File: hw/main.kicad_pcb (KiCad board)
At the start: 2 copper layers, 110 x 85 mm, 106 parts, among them J1 UART_01X03, J2 SWD_01X04, J3 SWD_01X04, J4 IDC_02X07, J5 IDC_02X07, J6 IDC_02X03, J7 IDC_02X13, J8 SMA, J9 IDC_02X05, SW1 LCD_BTN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

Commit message: updated pcb
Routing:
- net +5V: track 313.4 -> 312.7 mm

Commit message: updated pcb
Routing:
- net /Back/LED_PWM_R: track 239.6 -> 254.1 mm, vias 4 -> 8
- net /Back/LED_PWM_B: track 238.3 -> 246.7 mm, vias 7 -> 13
- net /Back/LED_PWM_G: track 225.5 -> 232.0 mm, vias 7 -> 13
- net +5V: track 312.7 -> 311.9 mm

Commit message: updated pcb
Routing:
- net +5V5: track 109.9 -> 107.6 mm

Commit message: updated pcb
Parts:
- added G***: LOGO, KLIB_Logo:wykys_skill, F.Cu at (147.0, 110.0)
- added REF**: Fiducial_Pad_1mm_Outer_2mm, KLIB_Mechanical:Fiducial_Pad_1mm_Outer_2mm, F.Cu at (190.0, 110.0)
- added REF**: Fiducial_Pad_1mm_Outer_2mm, KLIB_Mechanical:Fiducial_Pad_1mm_Outer_2mm, F.Cu at (190.0, 45.0)
- added REF**: Fiducial_Pad_1mm_Outer_2mm, KLIB_Mechanical:Fiducial_Pad_1mm_Outer_2mm, F.Cu at (90.0, 45.0)
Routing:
- net GND: vias 74 -> 78
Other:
- board text added: "LASER GAME MAIN BOARD V2"

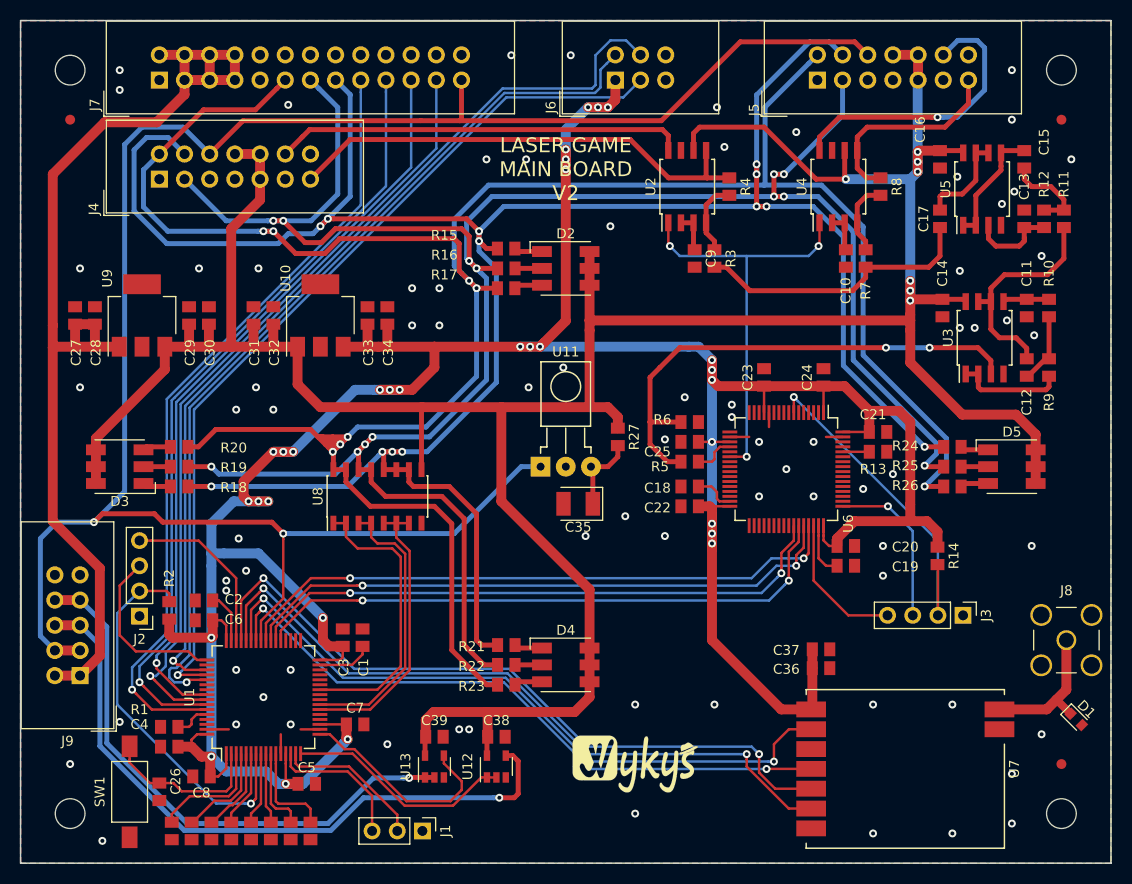
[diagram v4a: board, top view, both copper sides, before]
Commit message: removed LCD RST signal
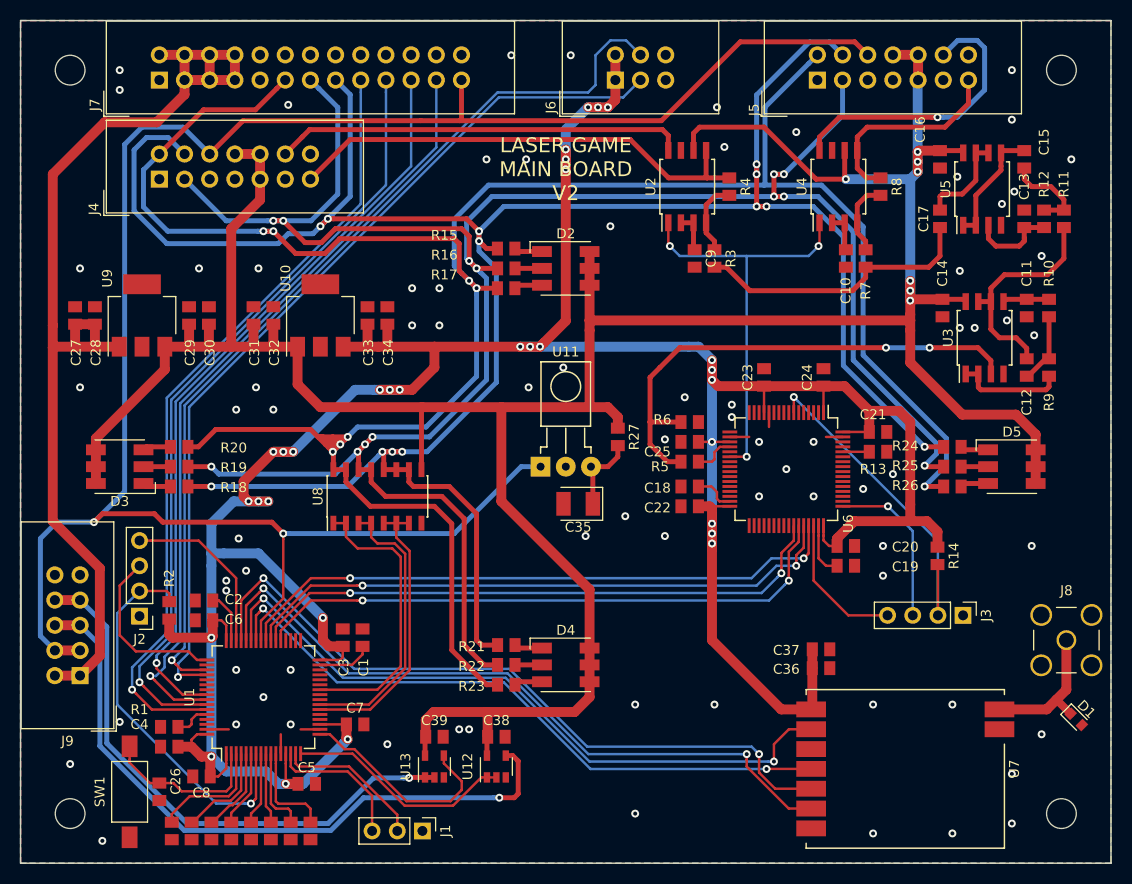
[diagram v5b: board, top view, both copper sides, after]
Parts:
- removed G***: LOGO, KLIB_Logo:wykys_skill
- removed REF** (x3): Fiducial_Pad_1mm_Outer_2mm, KLIB_Mechanical:Fiducial_Pad_1mm_Outer_2mm
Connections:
- J6 pad 2: /Display/~LCD_RST -> +3V3
- U1 pad 53: /Display/~LCD_RST -> Net-(U1-Pad53)
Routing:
- net /Display/~LCD_RST: track 91.2 -> 0.00 mm, vias 1 -> 0
- net +3V3: track 332.2 -> 334.7 mm
- net /Main MCU/LCD_UART_RX: track 89.2 -> 89.9 mm

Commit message: updated button RC filter
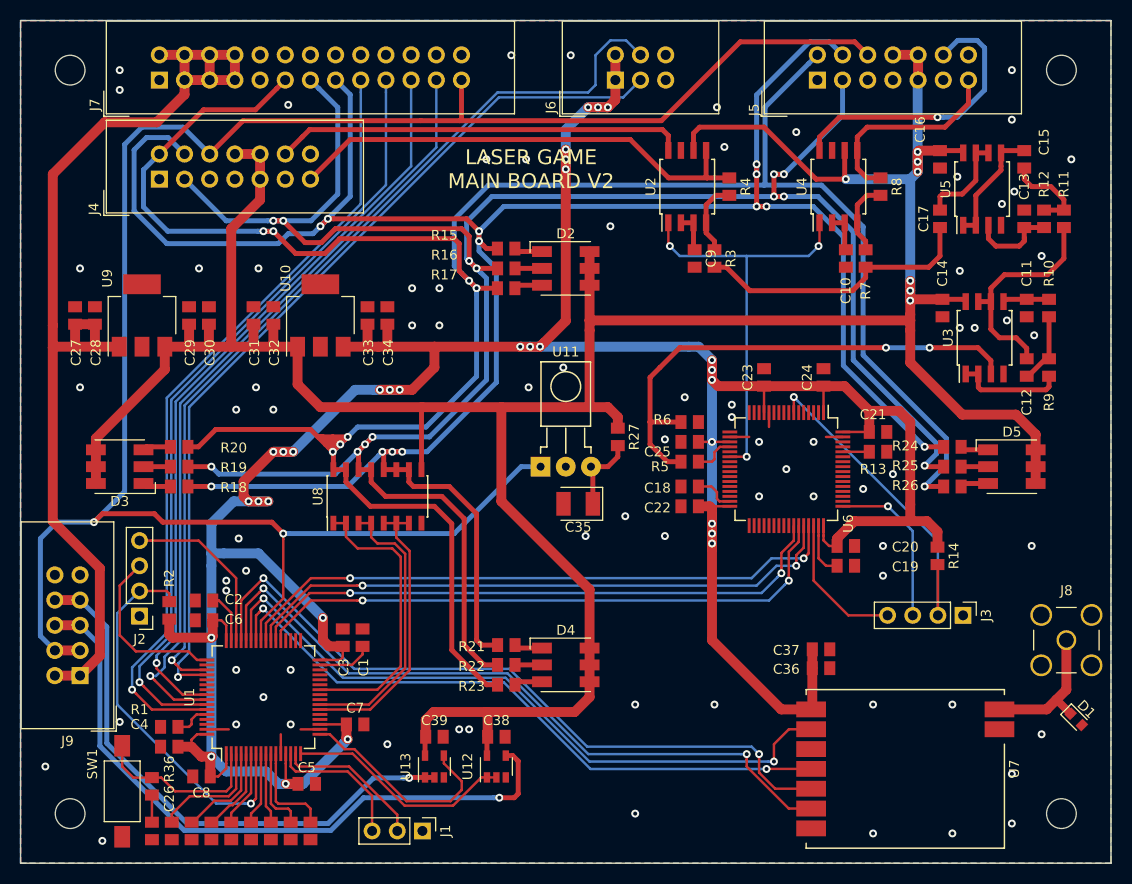
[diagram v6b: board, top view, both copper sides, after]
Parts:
- added R36: 100R, Resistor_SMD:R_0805_2012Metric, F.Cu at (98.2, 112.2)
- moved C26 4.02 mm to (98.2, 116.8)
- moved SW1 0.75 mm to (95.2, 112.8)
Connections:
- C26 pad 1: /Display/~BTN -> Net-(C26-Pad1)
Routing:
- net Net-(C26-Pad1): track 0.00 -> 2.74 mm
- net /Display/~BTN: track 16.6 -> 17.6 mm
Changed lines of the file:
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@@
     (tracks 1184)
     (zones 0)
-    (modules 106)
-    (nets 149)
+    (modules 107)
+    (nets 150)
   )
   (page A4)
@@
   (net 147 "Net-(U6-Pad15)")
   (net 148 "Net-(U1-Pad53)")
+  (net 149 "Net-(C26-Pad1)")
   (net_class Default "Toto je výchozí třída sítě."
     (clearance 0.2)
@@
     (add_net "Net-(C19-Pad1)")
     (add_net "Net-(C2-Pad1)")
+    (add_net "Net-(C26-Pad1)")
     (add_net "Net-(C35-Pad1)")
     (add_net "Net-(C9-Pad1)")
@@
     (add_net "Net-(U7-Pad7)")
   )
+  (module Resistor_SMD:R_0805_2012Metric (layer F.Cu)
+    (at 98.25 112.25 270)
+    (descr "Resistor SMD 0805 (2012 Metric), square (rectangular) end terminal, IPC_7351 nominal, (Body size source: http://www.tortai-tech.com/upload/download/2011102023233369053.pdf), generated with kicad-footprint-generator")
+    (tags resistor)
+    (attr smd)
+    (fp_text reference R36 (at -1.75 -1.75 270) (layer F.SilkS)
+      (effects (font (size 1 1) (thickness 0.15)))
+    )
+    (fp_text value 100R (at 0 1.65 270) (layer F.Fab)
+      (effects (font (size 1 1) (thickness 0.15)))
+    )
+    (fp_line (start -1 0.6) (end -1 -0.6) (layer F.Fab) (width 0.1))
+    (fp_line (start -1 -0.6) (end 1 -0.6) (layer F.Fab) (width 0.1))
+    (fp_line (start 1 -0.6) (end 1 0.6) (layer F.Fab) (width 0.1))
+    (fp_line (start 1 0.6) (end -1 0.6) (layer F.Fab) (width 0.1))
+    (fp_line (start -1.69 0.95) (end -1.69 -0.95) (layer F.CrtYd) (width 0.05))
+    (fp_line (start -1.69 -0.95) (end 1.69 -0.95) (layer F.CrtYd) (width 0.05))
+    (fp_line (start 1.69 -0.95) (end 1.69 0.95) (layer F.CrtYd) (width 0.05))
+    (fp_line (start 1.69 0.95) (end -1.69 0.95) (layer F.CrtYd) (width 0.05))
+    (fp_text user %R (at 0 0 270) (layer F.Fab)
+      (effects (font (size 0.5 0.5) (thickness 0.08)))
+    )
+    (pad 1 smd rect (at -0.88 0 270) (size 1.12 1.4) (layers F.Cu F.Paste F.Mask)
+      (net 100 /Display/~BTN))
+    (pad 2 smd rect (at 0.88 0 270) (size 1.12 1.4) (layers F.Cu F.Paste F.Mask)
+      (net 149 "Net-(C26-Pad1)"))
+    (model ${KISYS3DMOD}/Resistor_SMD.3dshapes/R_0805_2012Metric.wrl
+      (at (xyz 0 0 0))
+      (scale (xyz 1 1 1))
+      (rotate (xyz 0 0 0))
+    )
+  )
   (module Capacitor_SMD:C_0805_2012Metric (layer F.Cu)
     (at 133 107.25)
@@
   )
   (module Button_Switch_SMD:SW_SPST_FSMSM (layer F.Cu)
-    (at 96 112.8 270)
+    (at 95.25 112.75 270)
     (descr http://www.te.com/commerce/DocumentDelivery/DDEController?Action=srchrtrv&DocNm=1437566-3&DocType=Customer+Drawing&DocLang=English)
     (tags "SPST button tactile switch")
     (attr smd)
-    (fp_text reference SW1 (at 0 3 270) (layer F.SilkS)
+    (fp_text reference SW1 (at -2.75 3 270) (layer F.SilkS)
       (effects (font (size 1 1) (thickness 0.15)))
     )
@@
   )
   (module Capacitor_SMD:C_0805_2012Metric (layer F.Cu)
-    (at 99 112.8 270)
+    (at 98.25 116.75 270)
     (descr "Capacitor SMD 0805 (2012 Metric), square (rectangular) end terminal, IPC_7351 nominal, (Body size source: http://www.tortai-tech.com/upload/download/2011102023233369053.pdf), generated with kicad-footprint-generator")
     (tags capacitor)
     (attr smd)
-    (fp_text reference C26 (at -1.05 -1.65 270) (layer F.SilkS)
+    (fp_text reference C26 (at -3.25 -1.75 270) (layer F.SilkS)
       (effects (font (size 1 1) (thickness 0.15)))
     )
@@
       (net 2 GND))
     (pad 1 smd rect (at -0.88 0 270) (size 1.12 1.4) (layers F.Cu F.Paste F.Mask)
-      (net 100 /Display/~BTN))
+      (net 149 "Net-(C26-Pad1)"))
     (model ${KISYS3DMOD}/Capacitor_SMD.3dshapes/C_0805_2012Metric.wrl
       (at (xyz 0 0 0))
@@
     )
   )
-  (gr_text "LASER GAME\nMAIN BOARD\nV2" (at 140 50) (layer F.SilkS)
+  (gr_text "LASER GAME\nMAIN BOARD V2" (at 136.5 50) (layer F.SilkS)
     (effects (font (size 1.5 1.5) (thickness 0.3)))
   )
@@
   (segment (start 106.75 108.95) (end 106.75 112.5) (width 0.25) (layer F.Cu) (net 1))
   (segment (start 100.25 115.06) (end 100.25 115.87) (width 0.25) (layer F.Cu) (net 1))
+  (via (at 87.5 110.25) (size 0.8) (drill 0.4) (layers F.Cu B.Cu) (net 2))
   (via (at 122 108) (size 0.8) (drill 0.4) (layers F.Cu B.Cu) (net 2))
   (via (at 188 107) (size 0.8) (drill 0.4) (layers F.Cu B.Cu) (net 2))
@@
   (via (at 185 116) (size 0.8) (drill 0.4) (layers F.Cu B.Cu) (net 2))
   (via (at 191 49) (size 0.8) (drill 0.4) (layers F.Cu B.Cu) (net 2))
-  (via (at 90 110) (size 0.8) (drill 0.4) (layers F.Cu B.Cu) (net 2))
   (via (at 185 45) (size 0.8) (drill 0.4) (layers F.Cu B.Cu) (net 2))
   (via (at 185 40) (size 0.8) (drill 0.4) (layers F.Cu B.Cu) (net 2))
@@
   (segment (start 120.46 113.21) (end 120.46 116.75) (width 0.25) (layer F.Cu) (net 99))
   (segment (start 112.25 110.25) (end 112.75 110.75) (width 0.25) (layer F.Cu) (net 99))
-  (segment (start 99 111.92) (end 98.05 111.92) (width 0.25) (layer F.Cu) (net 100))
-  (segment (start 98.05 111.92) (end 96 109.87) (width 0.25) (layer F.Cu) (net 100))
-  (segment (start 96 109.87) (end 96 109.55) (width 0.25) (layer F.Cu) (net 100))
-  (segment (start 96 109.55) (end 96 108.21) (width 0.25) (layer F.Cu) (net 100))
-  (segment (start 101.25 112.75) (end 100.42 111.92) (width 0.25) (layer F.Cu) (net 100))
-  (segment (start 105.75 112.75) (end 101.25 112.75) (width 0.25) (layer F.Cu) (net 100))
-  (segment (start 106.25 112.25) (end 105.75 112.75) (width 0.25) (layer F.Cu) (net 100))
-  (segment (start 106.25 108.95) (end 106.25 112.25) (width 0.25) (layer F.Cu) (net 100))
-  (segment (start 100.42 111.92) (end 99 111.92) (width 0.25) (layer F.Cu) (net 100))
+  (segment (start 98.25 111.37) (end 96.37 111.37) (width 0.25) (layer F.Cu) (net 100))
+  (segment (start 96.37 111.37) (end 95.25 110.25) (width 0.25) (layer F.Cu) (net 100))
+  (segment (start 95.25 110.25) (end 95.25 108.16) (width 0.25) (layer F.Cu) (net 100))
+  (segment (start 105.75 112.75) (end 106.25 112.25) (width 0.25) (layer F.Cu) (net 100))
+  (segment (start 100.58 112.75) (end 105.75 112.75) (width 0.25) (layer F.Cu) (net 100))
+  (segment (start 99.2 111.37) (end 100.58 112.75) (width 0.25) (layer F.Cu) (net 100))
+  (segment (start 98.25 111.37) (end 99.2 111.37) (width 0.25) (layer F.Cu) (net 100))
+  (segment (start 106.25 112.25) (end 106.25 108.95) (width 0.25) (layer F.Cu) (net 100))
   (segment (start 190.934315 104.934315) (end 189.5 103.5) (width 0.8) (layer F.Cu) (net 101))
   (segment (start 189.5 103.5) (end 190.5 102.5) (width 1) (layer F.Cu) (net 101))
@@
   (via (at 133.3 113.4) (size 0.8) (drill 0.4) (layers F.Cu B.Cu) (net 145))
   (segment (start 88.46 96) (end 91 96) (width 1) (layer F.Cu) (net 145))
+  (segment (start 98.25 115.87) (end 98.25 113.13) (width 0.25) (layer F.Cu) (net 149))
   (zone (net 2) (net_name GND) (layer F.Cu) (hatch edge 0.508)
     (connect_pads (clearance 0.508))

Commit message: added fiducials
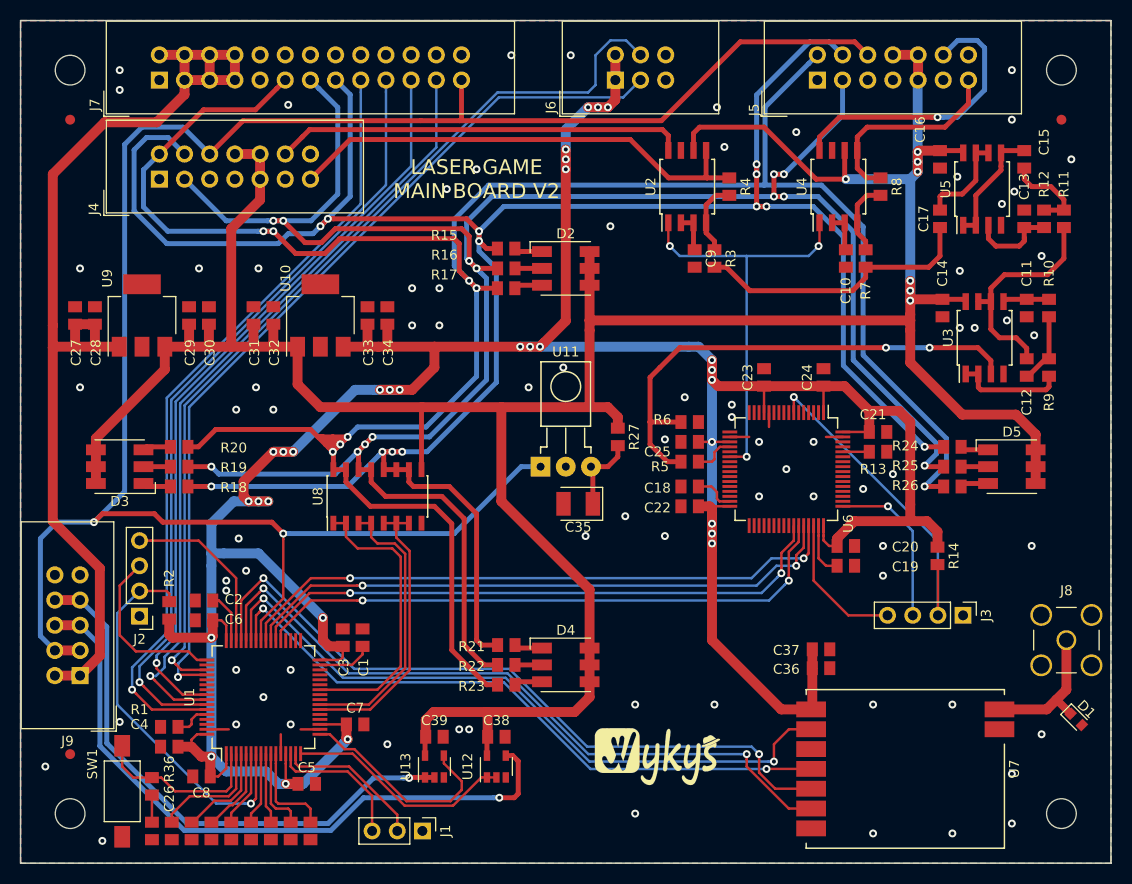
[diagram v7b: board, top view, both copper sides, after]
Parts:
- added G***: LOGO, KLIB_Logo:wykys_skill, F.Cu at (149.2, 109.2)
- added REF**: Fiducial_Pad_1mm_Outer_2mm, KLIB_Mechanical:Fiducial_Pad_1mm_Outer_2mm, F.Cu at (90.0, 45.0)
- added REF**: Fiducial_Pad_1mm_Outer_2mm, KLIB_Mechanical:Fiducial_Pad_1mm_Outer_2mm, F.Cu at (190.0, 45.0)
- added REF**: Fiducial_Pad_1mm_Outer_2mm, KLIB_Mechanical:Fiducial_Pad_1mm_Outer_2mm, F.Cu at (90.0, 109.0)
